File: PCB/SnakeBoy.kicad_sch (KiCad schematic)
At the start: 23 parts, among them SW1 X, SW2 A, SW3 Y, SW4 B, SW5 Start, SW6 Select, SW7 Power_SW, U1 ESP32-S3-DEVKITC-1-N16R8, U2 Joystick, U3 PAM8304 Module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

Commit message: Finished tracing the PCB
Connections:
- net 3v3+: now also A1.1R (VCC); no longer A1.6R (VCC)
- net 3v7-: now also A1.2R (GND); no longer A1.8R (GND)
- net TFT_BL: now also A1.8R (TFT_BL), U1.J1_7 (GPIO7); no longer A1.7R (TFT_BL), U1.J1_4 (GPIO4)
- net TFT_CLK: now also A1.7R (TFT_CLK), U1.J1_6 (GPIO6); no longer A1.5R (TFT_CLK), U1.J1_5 (GPIO5)
- net TFT_CS: now also A1.3R (TFT_~{CS}); no longer A1.2R (TFT_~{CS})
- net TFT_DC: now also A1.5R (TFT_D~{C}), U1.J1_4 (GPIO4); no longer A1.3R (TFT_D~{C}), U1.J1_7 (GPIO7)
- net TFT_DIN: now also A1.6R (TFT_DIN), U1.J1_5 (GPIO5); no longer A1.4R (TFT_DIN), U1.J1_6 (GPIO6)
- net TFT_RST: now also A1.4R (TFT_~{RST}); no longer A1.1R (TFT_~{RST})

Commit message: Cloning the firmware source code from "@retroelec"
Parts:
- RV1: footprint slider:PS45M0MC2BR10KN -> Potentiometer_THT:Potentiometer_Bourns_PTV112-4_Dual_Vertical
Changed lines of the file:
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@@
 			)
 		)
-		(property "Footprint" "slider:PS45M0MC2BR10KN"
+		(property "Footprint" "Potentiometer_THT:Potentiometer_Bourns_PTV112-4_Dual_Vertical"
 			(at 135.89 56.515 0)
 			(effects

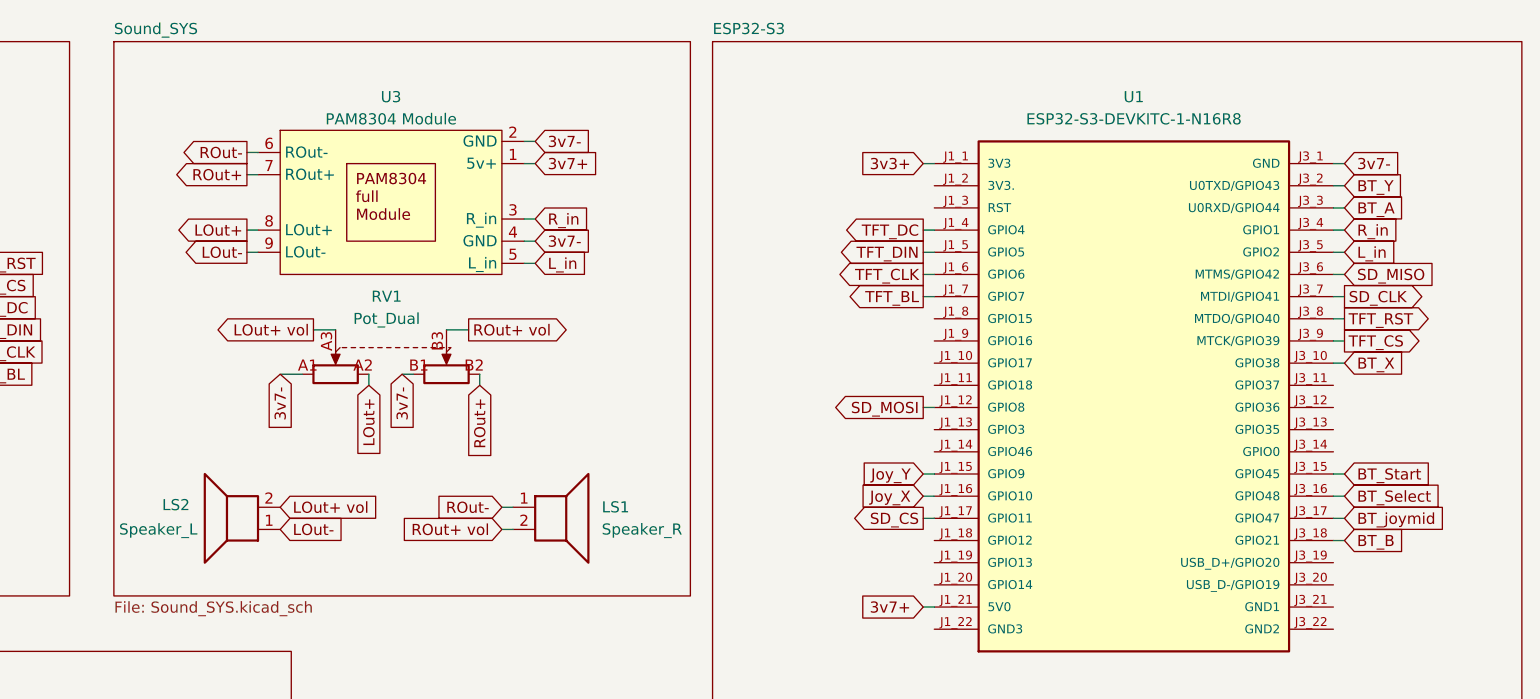
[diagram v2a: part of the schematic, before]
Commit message: Edited the PCB to match the firmware
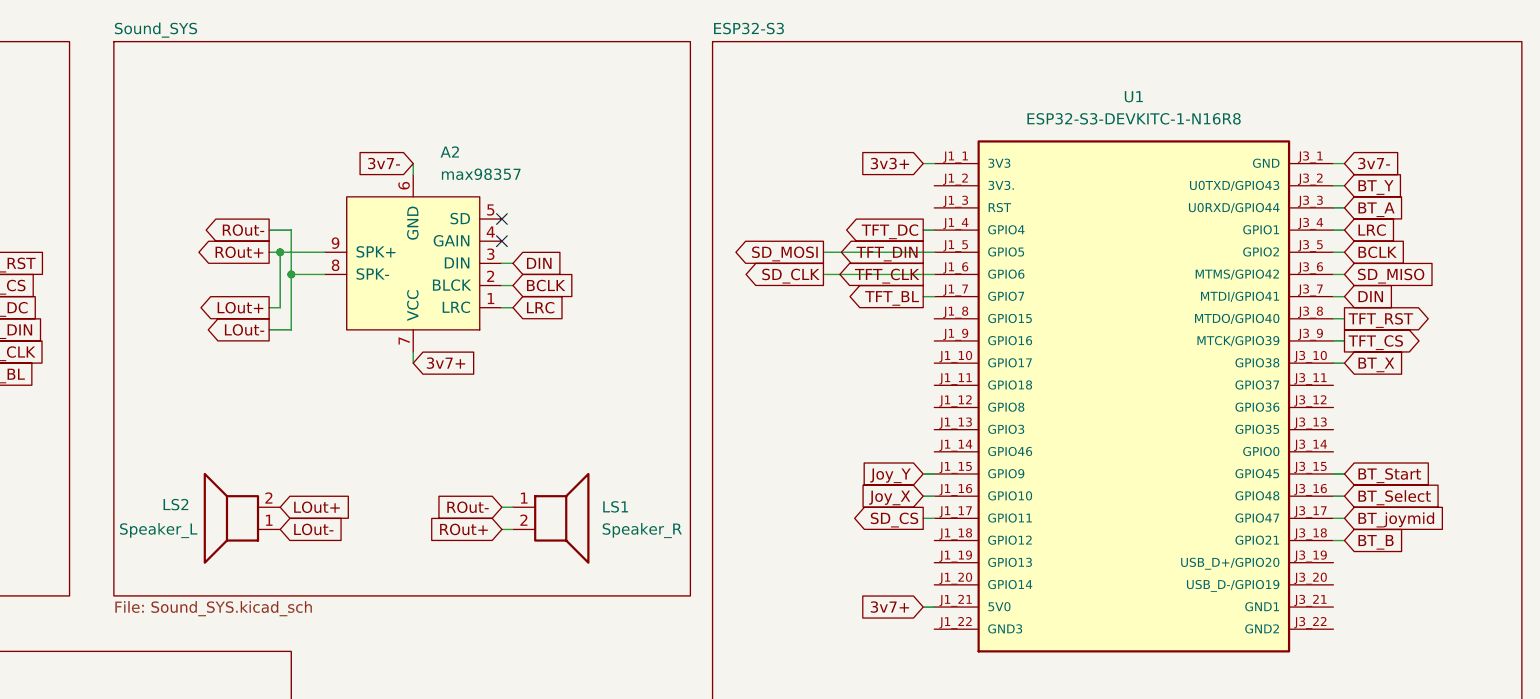
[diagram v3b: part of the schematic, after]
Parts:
- removed RV1: Pot_Dual, Potentiometer_THT:Potentiometer_Bourns_PTV112-4_Dual_Vertical, symbol Device:R_Potentiometer_Dual
- removed U3: PAM8304 Module, RAM:PAM8403, symbol RAM-Components:PAM8304_Module
- added A2: max98357, Module-extra:max98357, symbol Module-extra:max98357
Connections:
- net LOut+ vol is gone; now on net LOut+: LS2.2
- net ROut+ vol is gone; now on net LOut+: LS1.2
- net ROut- is gone; now on net LOut-: LS1.1
- net TFT_CLK is gone; now on net SD_CLK: A1.7R (TFT_CLK), U1.J1_6 (GPIO6)
- net TFT_DIN is gone; now on net SD_MOSI: A1.6R (TFT_DIN), U1.J1_5 (GPIO5)
- net 3v7+: now also A2.7 (VCC)
- net 3v7-: now also A2.6 (GND)
- net LOut+: now also A2.9 (SPK+)
- net LOut-: now also A2.8 (SPK-)
- net SD_CLK: no longer U1.J3_7 (MTDI/GPIO41)
- net SD_MOSI: no longer U1.J1_12 (GPIO8)
- net L_in renamed BCLK
- net BCLK: now also A2.2 (BLCK)
- net R_in renamed LRC
- net LRC: now also A2.1 (LRC)
- new net DIN: A2.3 (DIN), U1.J3_7 (MTDI/GPIO41)
- no-connect marks 0 -> 2
